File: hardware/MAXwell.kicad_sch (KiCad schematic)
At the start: 87 parts, among them J2 Conn_02x12_Counter_Clockwise, U1 EPM240T100, U2 AMS1117-3.3, U3 D168K, U4 D168K, U5 D168K, U6 D168K, X1 50.000, X2 14.756

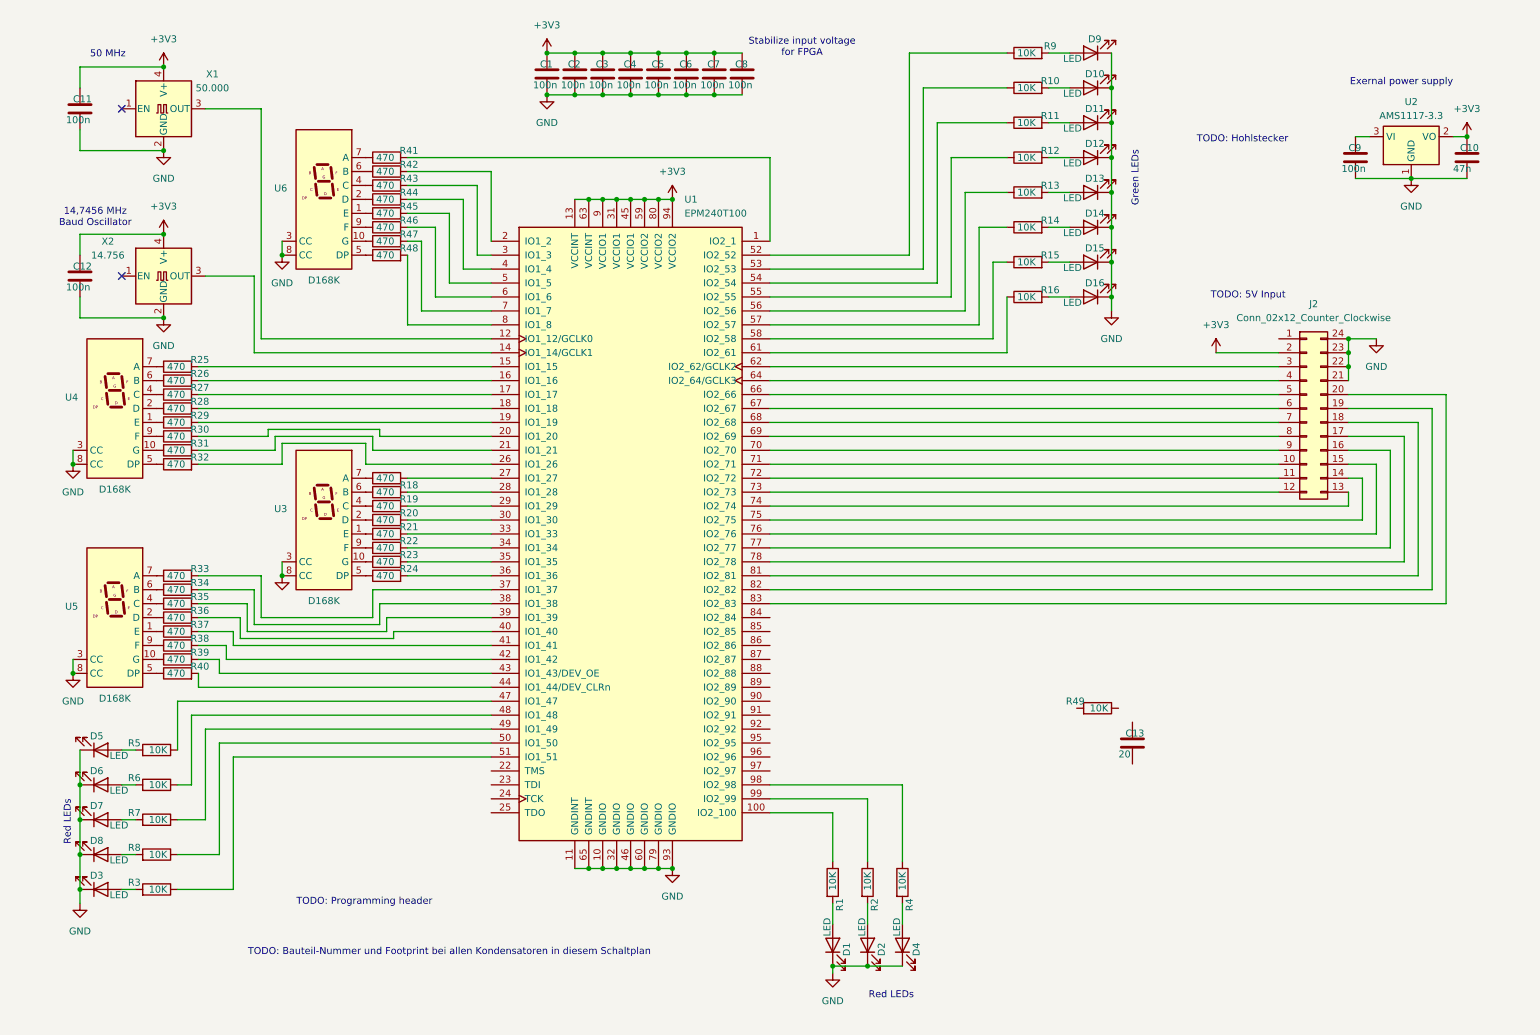
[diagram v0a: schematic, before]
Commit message: restructure + buttons added
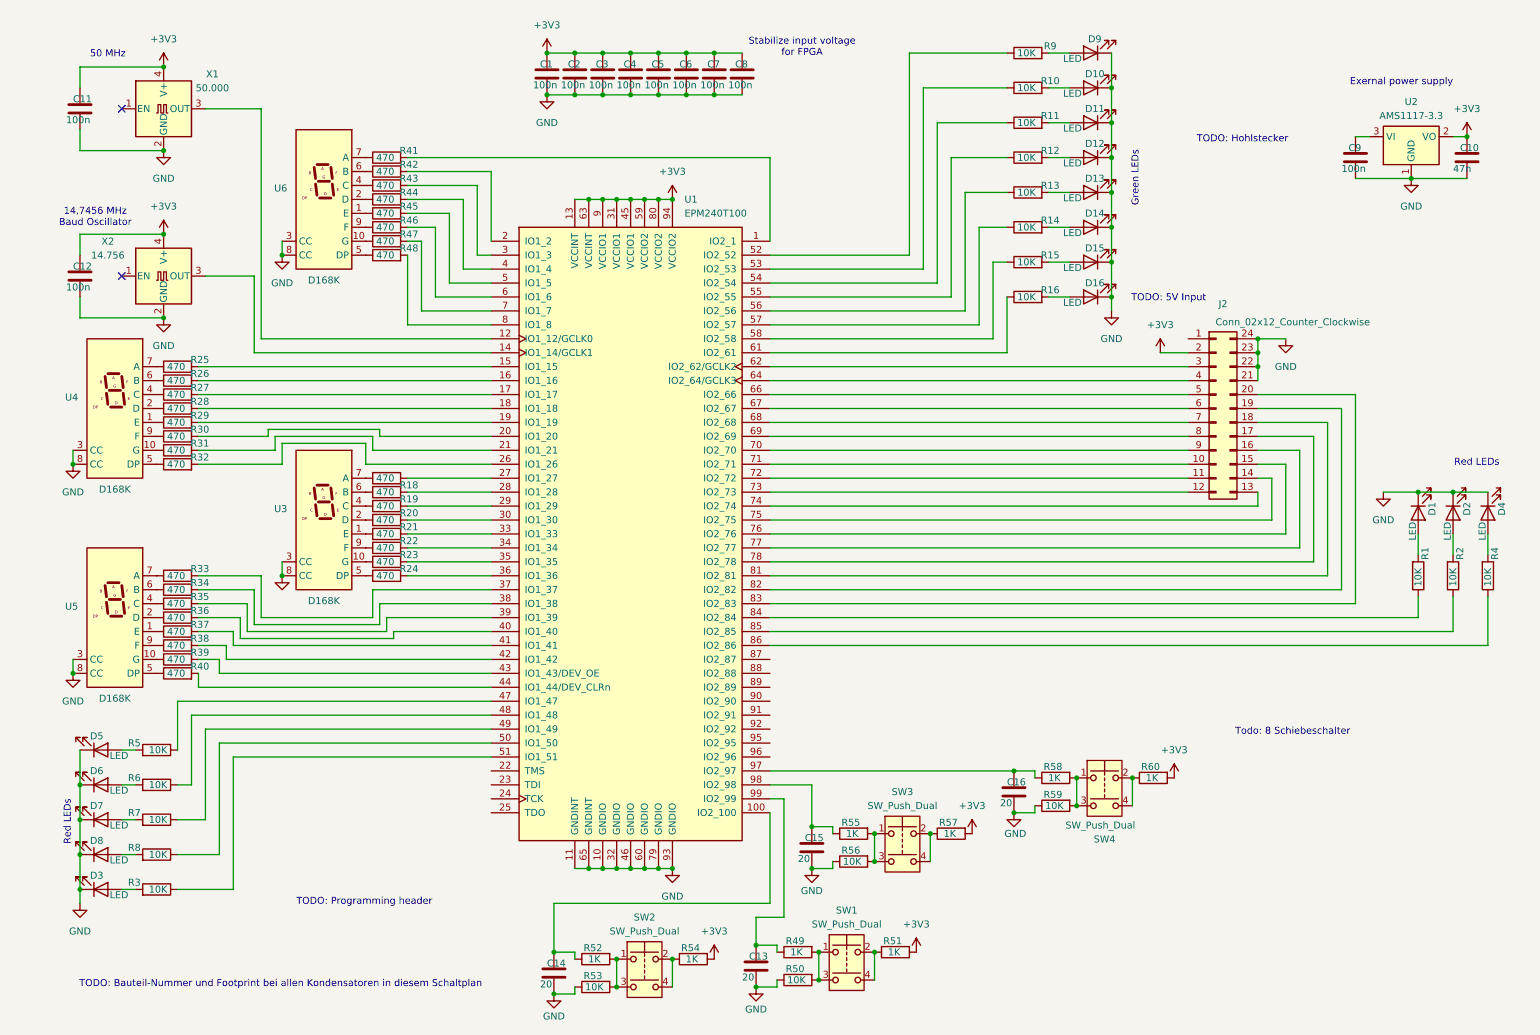
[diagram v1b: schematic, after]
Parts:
- added C14, C15, C16: 20, symbol Device:C
- added R50, R53, R56, R59: 10K, symbol Device:R
- added R51, R52, R54, R55, R57, R58, R60: 1K, symbol Device:R
- added SW1, SW2, SW3, SW4: SW_Push_Dual, Button_Switch_THT:SW_PUSH-12mm, symbol Switch:SW_Push_Dual
- R49: value 10K -> 1K; Part-Nr (none) -> OMR B3F-4000
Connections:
- net +3V3: now also R51.2, R54.2, R57.2, R60.2
- net GND: now also C13.2, C14.2, C15.2, C16.2, R50.1, R53.1, R56.1, R59.1
- net at U1.100 (IO2_100): now also C14.1, R52.1; no longer R1.1
- net at U1.84 (IO2_84): now also R1.1
- net at U1.85 (IO2_85): now also R2.1
- net at U1.86 (IO2_86): now also R4.1
- net at U1.97 (IO2_97): now also C16.1, R58.1
- net at U1.98 (IO2_98): now also C15.1, R55.1; no longer R4.1
- net at U1.99 (IO2_99): now also C13.1, R49.1; no longer R2.1
- net at R49.2: now also R50.2, SW1.1, SW1.3
- new net: R60.1, SW4.2, SW4.4
- new net: R55.2, R56.2, SW3.1, SW3.3
- new net: R58.2, R59.2, SW4.1, SW4.3
- new net: R54.1, SW2.2, SW2.4
- new net: R51.1, SW1.2, SW1.4
- new net: R52.2, R53.2, SW2.1, SW2.3
- new net: R57.1, SW3.2, SW3.4
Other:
- note added: "Todo: 8 Schiebeschalter"
- moved on the sheet: C13, D1, D2, D4, J2, R1, R2, R4, R49

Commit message: restructured » more Space
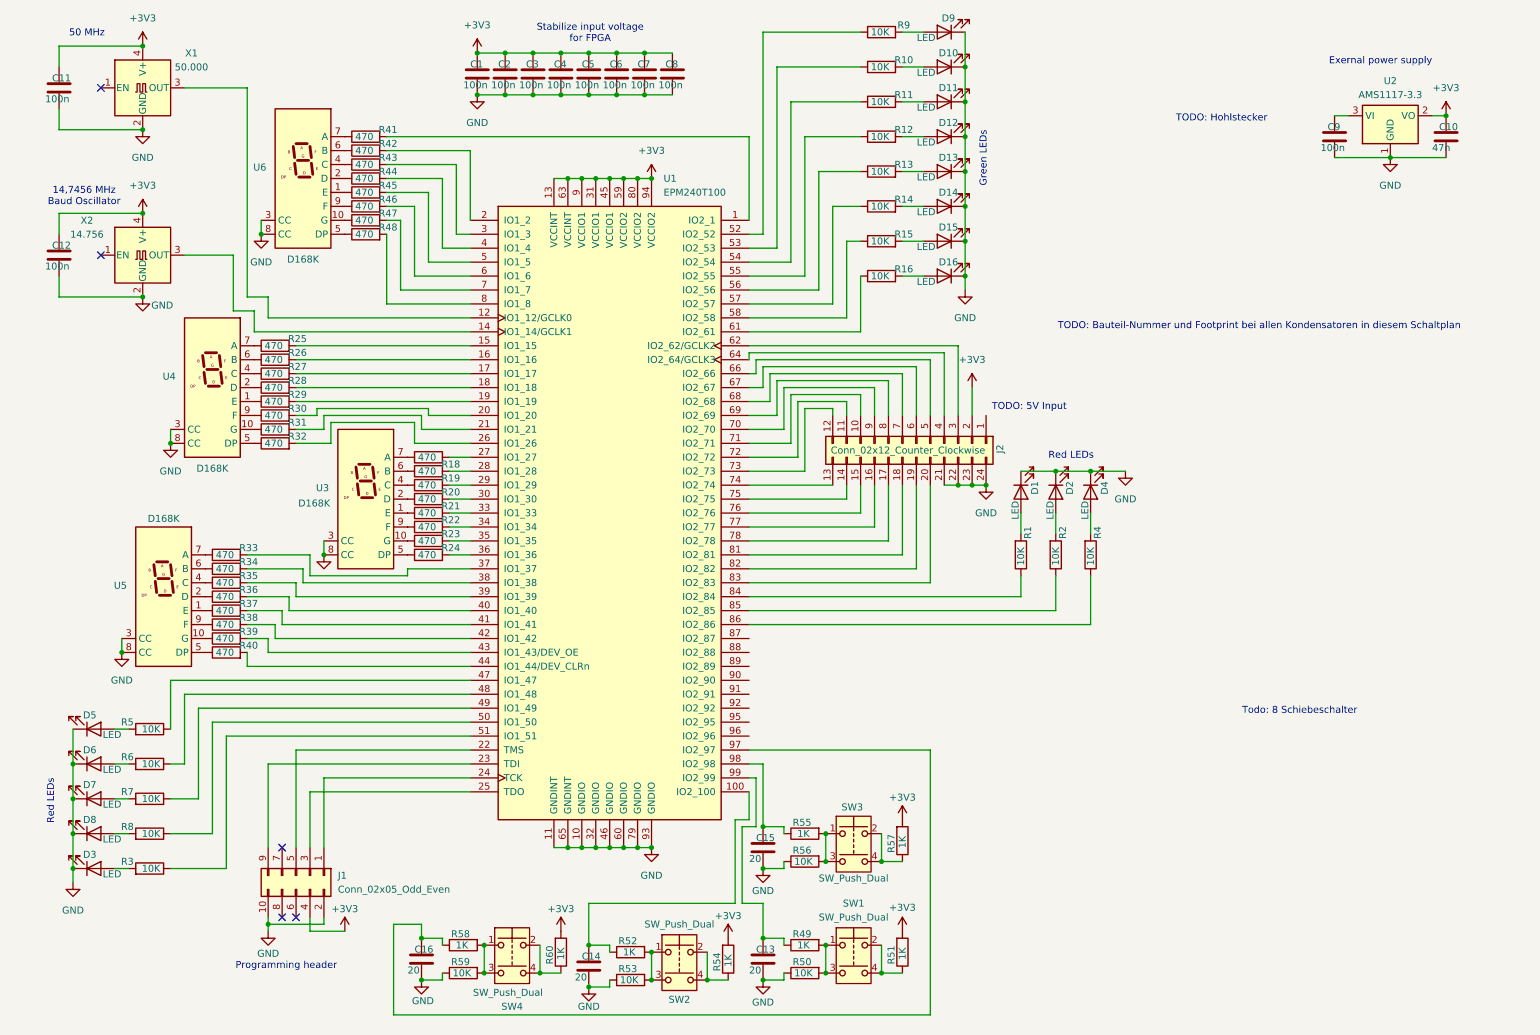
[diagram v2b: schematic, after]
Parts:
- added J1: Conn_02x05_Odd_Even, Connector_IDC:IDC-Header_2x05_P2.54mm_Vertical, symbol Connector_Generic:Conn_02x05_Odd_Even
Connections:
- net +3V3: now also J1.4 (Pin_4)
- net GND: now also J1.10 (Pin_10), J1.2 (Pin_2)
- net at U1.22 (TMS): now also J1.5 (Pin_5)
- net at U1.23 (TDI): now also J1.9 (Pin_9)
- net at U1.24 (TCK): now also J1.1 (Pin_1)
- net at U1.25 (TDO): now also J1.3 (Pin_3)
- no-connect marks 2 -> 5
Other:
- note added: "Programming header"
- note removed: "TODO: Programming header"
- moved on the sheet: C1, C10, C11, C12, C13, C14, C15, C16, C2, C3, C4, C5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

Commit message: all objects placed, footprint assignment missing
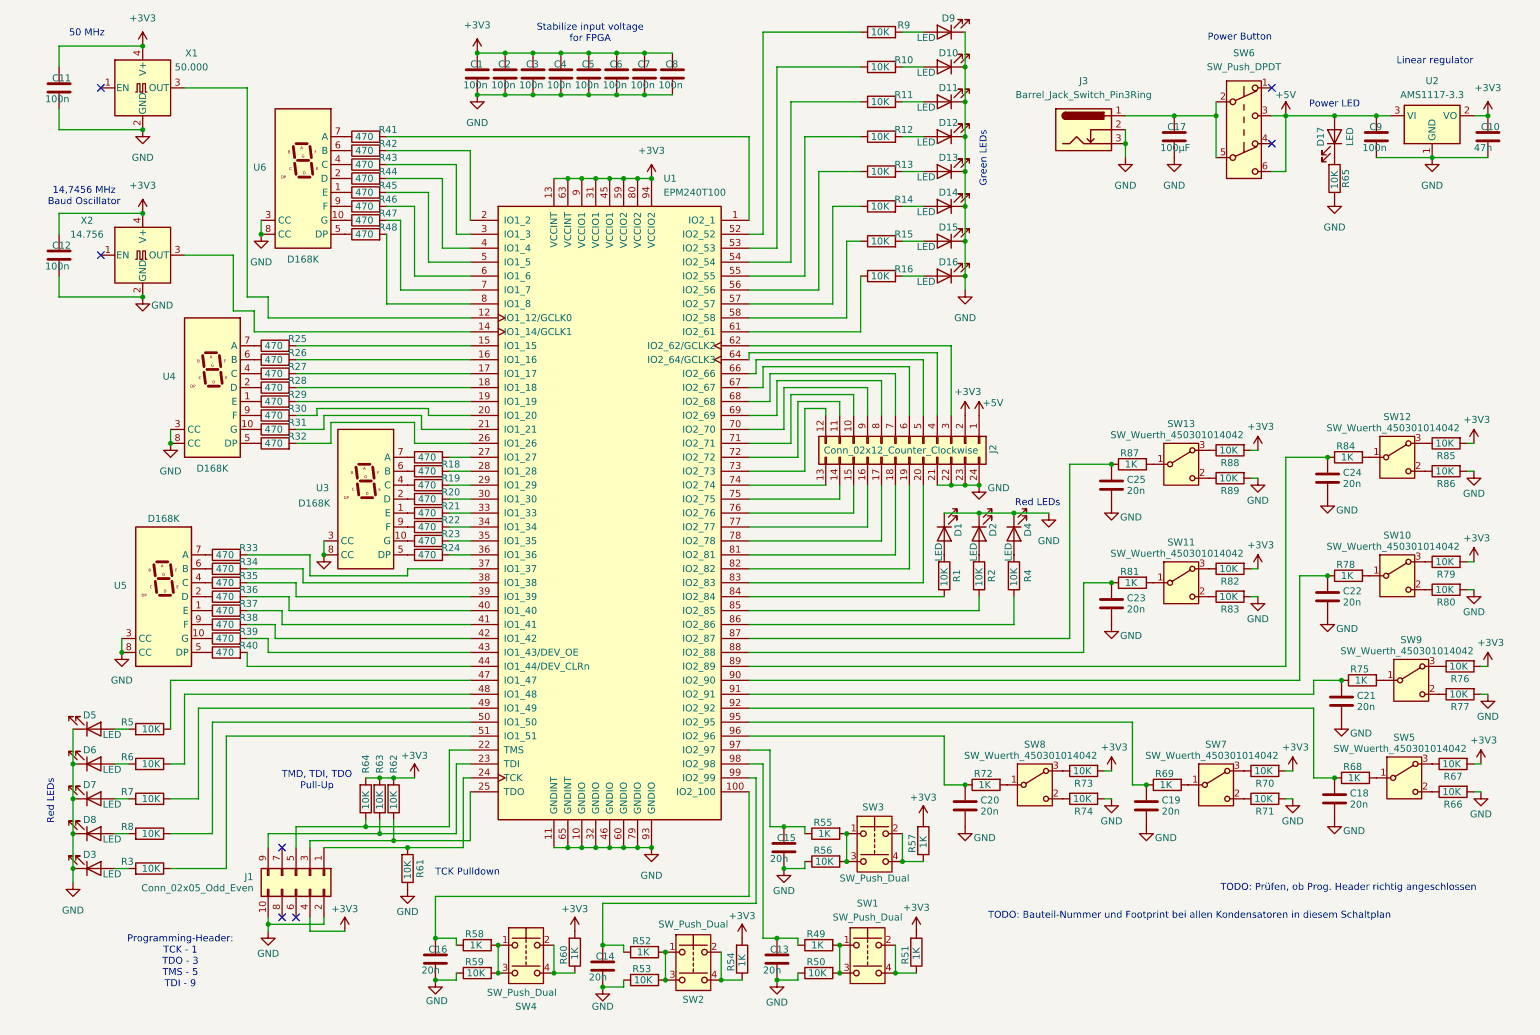
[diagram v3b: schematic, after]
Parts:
- added C17: 100µF, symbol Device:C
- added C18, C19, C20, C21, C22, C23, C24, C25: 20n, symbol Device:C
- added D17: LED, symbol Device:LED
- added J3: Barrel_Jack_Switch_Pin3Ring, Connector_BarrelJack:BarrelJack_CUI_PJ-063AH_Horizontal_CircularHoles, symbol Connector:Barrel_Jack_Switch_Pin3Ring
- added R61, R62, R63, R64, R65, R66, R67, R70, R71, R73, R74, R76, R77, R79, R80, R82, R83, R85, R86, R88, R89: 10K, symbol Device:R
- added R68, R69, R72, R75, R78, R81, R84, R87: 1K, symbol Device:R
- added SW10, SW11, SW12, SW13, SW5, SW7, SW8, SW9: SW_Wuerth_450301014042, Button_Switch_THT:SW_Slide-03_Wuerth-WS-SLTV_10x2.5x6.4_P2.54mm, symbol Switch:SW_Wuerth_450301014042
- added SW6: SW_Push_DPDT, symbol Switch:SW_Push_DPDT
- C13, C14, C15, C16: value 20 -> 20n
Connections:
- net +3V3: now also R62.2, R63.2, R64.2, R67.2, R70.2, R73.2, R76.2, R79.2, R82.2, R85.2, R88.2
- net GND: now also C17.2, C18.2, C19.2, C20.2, C21.2, C22.2, C23.2, C24.2, C25.2, J3.2, J3.3, R61.1, R65.1, R66.2, R71.2, R74.2, R77.2, R80.2, R83.2, R86.2, R89.2
- net at C16.1, R58.1: now also U1.100 (IO2_100); no longer U1.97 (IO2_97)
- net at J1.1 (Pin_1), U1.24 (TCK): now also R61.2
- net at J1.3 (Pin_3), U1.25 (TDO): now also R62.1
- net at J1.5 (Pin_5), U1.22 (TMS): now also R64.1
- net at J1.9 (Pin_9), U1.23 (TDI): now also R63.1
- net at C14.1, R52.1: now also U1.99 (IO2_99); no longer U1.100 (IO2_100)
- net at U1.87 (IO2_87): now also C25.1, R87.1
- net at U1.88 (IO2_88): now also C23.1, R81.1
- net at U1.89 (IO2_89): now also C24.1, R84.1
- net at U1.90 (IO2_90): now also C22.1, R78.1
- net at U1.91 (IO2_91): now also C21.1, R75.1
- net at U1.92 (IO2_92): now also C18.1, R68.1
- net at U1.95 (IO2_95): now also C19.1, R69.1
- net at U1.96 (IO2_96): now also C20.1, R72.1
- net at C15.1, R55.1: now also U1.97 (IO2_97); no longer U1.98 (IO2_98)
- net at C13.1, R49.1: now also U1.98 (IO2_98); no longer U1.99 (IO2_99)
- net +5V: now reaches C9.1, U2.3 (VI)
- net +5V: now also J2.1 (Pin_1), D17.2 (A), SW6.3 (C), SW6.6 (C)
- new net: R84.2, SW12.1 (B)
- new net: R86.1, SW12.2 (C)
- new net: R85.1, SW12.3 (A)
- new net: R69.2, SW7.1 (B)
- new net: R71.1, SW7.2 (C)
- new net: R70.1, SW7.3 (A)
- new net: R81.2, SW11.1 (B)
- new net: R78.2, SW10.1 (B)
- new net: R68.2, SW5.1 (B)
- new net: R83.1, SW11.2 (C)
- new net: R82.1, SW11.3 (A)
- new net: C17.1, J3.1, SW6.2 (B), SW6.5 (B)
- new net: R76.1, SW9.3 (A)
- new net: R89.1, SW13.2 (C)
- new net: R88.1, SW13.3 (A)
- new net: R87.2, SW13.1 (B)
- new net: R73.1, SW8.3 (A)
- new net: R74.1, SW8.2 (C)
- new net: R75.2, SW9.1 (B)
- new net: R72.2, SW8.1 (B)
- new net: R66.1, SW5.2 (C)
- new net: R79.1, SW10.3 (A)
- new net: R67.1, SW5.3 (A)
- new net: D17.1 (K), R65.2
- new net: R80.1, SW10.2 (C)
- new net: R77.1, SW9.2 (C)
- no-connect marks 5 -> 7
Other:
- note added: "Linear regulator"
- note added: "Power Button"
- note added: "Power LED"
- note added: "Programming-Header: TCK - 1 TDO - 3 TMS - 5 TDI - 9"
- note added: "TCK Pulldown"
- note added: "TMD, TDI, TDO Pull-Up"
- note added: "TODO: Prüfen, ob Prog. Header richtig angeschlossen"
- note removed: "Exernal power supply"
- note removed: "Programming header"
- note removed: "TODO: 5V Input"
- note removed: "TODO: Hohlstecker"
- note removed: "Todo: 8 Schiebeschalter"
- moved on the sheet: C10, C13, C14, C15, C16, C9, D1, D2, D4, J2, R1, R2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
